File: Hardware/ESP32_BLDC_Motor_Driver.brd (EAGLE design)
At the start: 85.1 x 61 mm, 189 parts, among them J1 USB-C Connector, J2 0532610371, J3 POWER_JACKPOWER_JACK_SLOT, J4 Breadboard Connector, J5 Breadboard Headers, J6 0.1in header, J7 QWIIC_RIGHT_ANGLE, J8 Breakout Header, Q1 20V/4.2A/52mΩ/1.4W, Q2 NPN Transistors, U1 TMC6300, U3 ESP-WROOM-3232D, U4 CH340C, U5 ESD Diode, U6 AP63357, U7 AP2202-ADJ, U8 TMAG5273, U9 LMV324

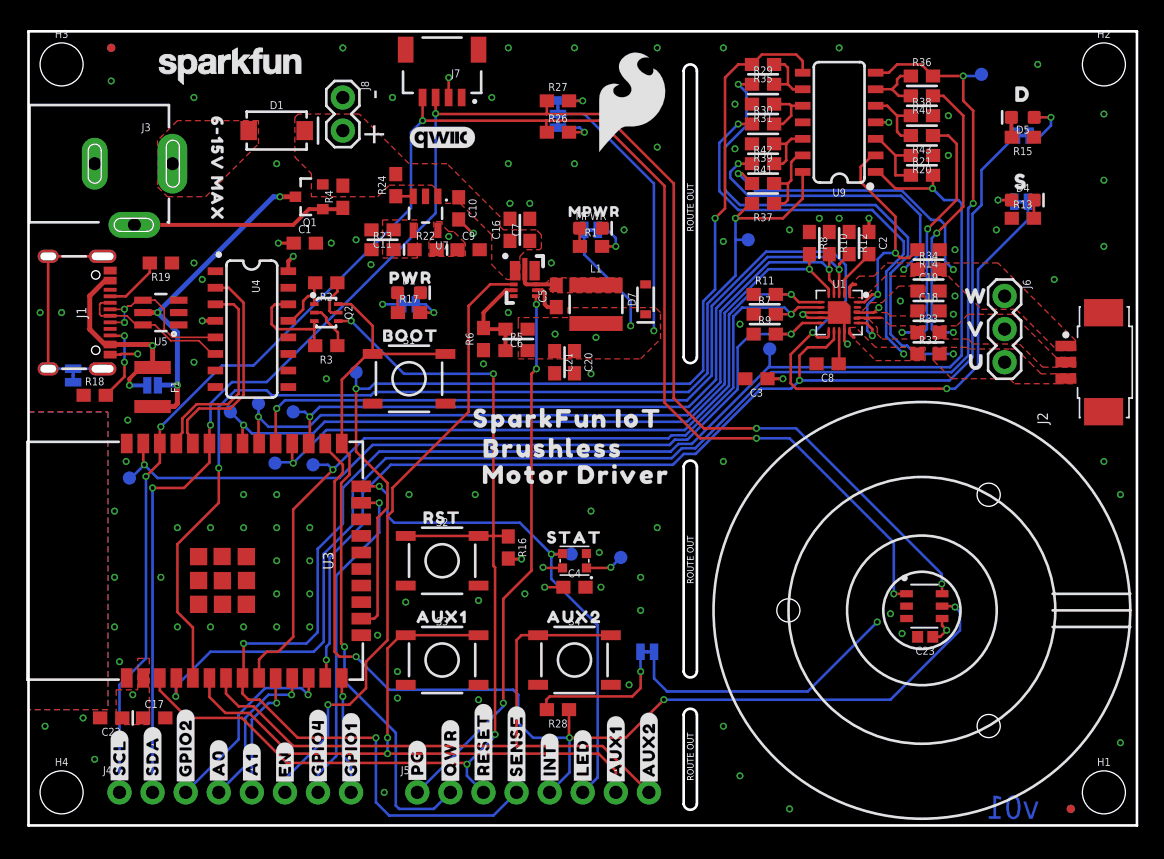
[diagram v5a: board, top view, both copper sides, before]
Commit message: Design review changes
Updated datasheets with correct parts in it now; removed power jack; changed direction of motor and output connector to the motor; swapped resistances of op amp for inline current sensing; updated sizes of some resistances; fixed power scheme of the board; added perfect diode circuit; for more information, see protos review doc
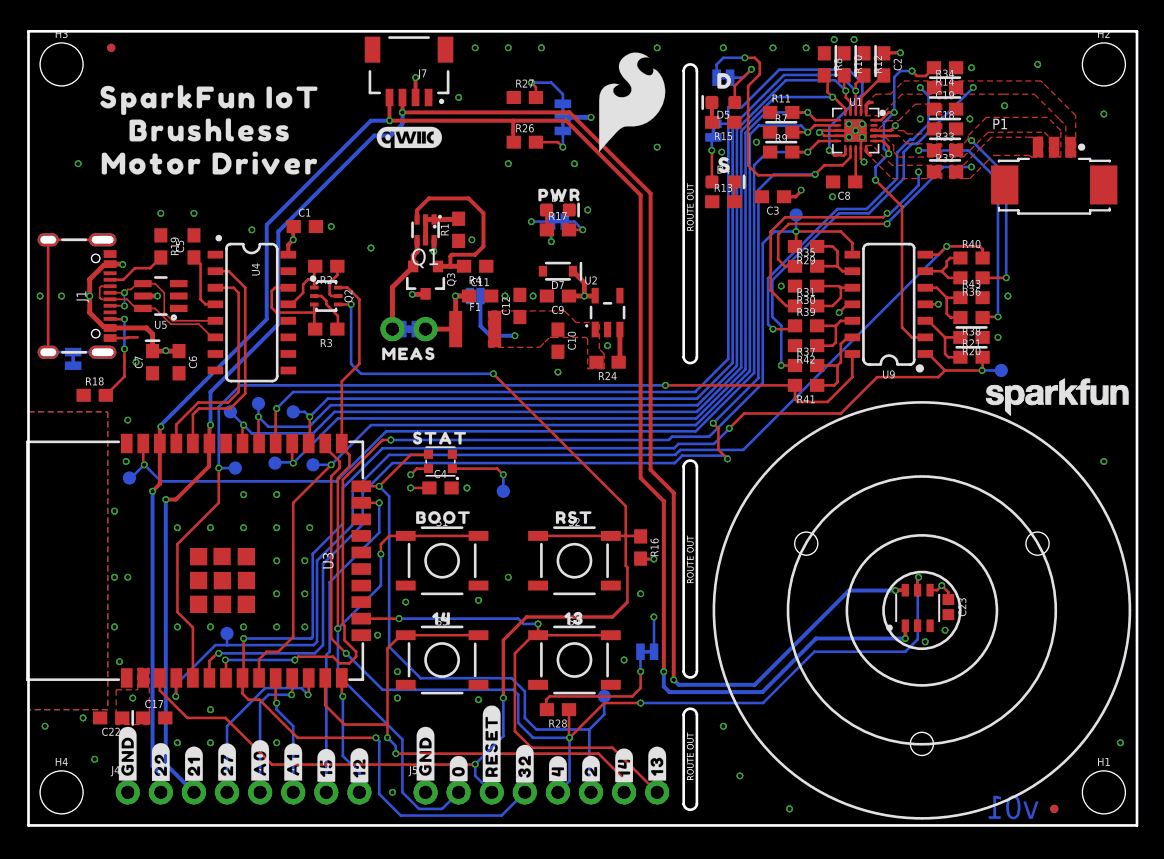
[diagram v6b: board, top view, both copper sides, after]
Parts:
- removed C16: 10uF, SparkFun-Capacitors:0603
- removed C20, C21: 22uF, SparkFun-Capacitors:0603
- removed D1: 1A/40V/500mV, SparkFun-DiscreteSemi:SMA-DIODE
- removed J2: 0532610371, 0532610371:MOLEX_0532610371
- removed J3: POWER_JACKPOWER_JACK_SLOT, SparkFun-Connectors:POWER_JACK_PTH_SLOT
- removed J6: 0.1in header, SparkFun-Connectors:1X03
- removed J8: Breakout Header, SparkFun-Connectors:1X02
- removed L1: 4.7μH, SparkFun-Coils:INDUCTOR_4X4MM
- removed MOTOR: JUMPER-SMT_2_NC_TRACE_SILK, SparkFun-Jumpers:SMT-JUMPER_2_NC_TRACE_SILK
- removed MPWR: RED, SparkFun-LED:LED-0603
- removed R22: 16.2k, SparkFun-Resistors:0603
- removed R23: 26.7k, SparkFun-Resistors:0603
- removed R5: 93.1k, SparkFun-Resistors:0603
- removed R6: 30.1k, SparkFun-Resistors:0603
- removed U$49, U$57: (no value), output:U630063003494
- removed U$50, U$60: (no value), output:V630063003496
- removed U$51, U$61: (no value), output:W630063003497
- removed U$55: (no value), output:#SDA#28
- removed U$58: (no value), output:#SCL#29
- removed U6: AP63357, SparkFun-IC-Power:V-DFN3020-13
- removed U7: AP2202-ADJ, SparkFun-IC-Power:SOT23-5
- added C12: 0.1uF, SparkFun-Capacitors:0603
- added MEAS: JUMPER-COMBO_2_NC_TRACE, SparkFun-Jumpers:COMBO-JUMPER_2_NC_TRACE
- added P1: 0532610371, 0532610371:MOLEX_0532610371
- added Q3: 20V/4.2A/52mΩ/1.4W, SparkFun-DiscreteSemi:SOT23-3
- added U2: 3.3V, SparkFun-IC-Power:SOT23-5
- C11: value 100pF -> 0.1uF
- C5: value 0.1uF -> 10nF
- C6: value 33pF -> 0.1uF
- C7: device SparkFun-Capacitors:0603 -> SparkFun-Capacitors:0603-POLAR
- Q1: value 20V/4.2A/52mΩ/1.4W -> (none); device SparkFun-DiscreteSemi:SOT23-3 -> SparkFun-DiscreteSemi:SOT363_PHILIPS
- R1: value 4.7k -> 100k
- R4: value 100k -> 1M
- U$10: device output:#34#AUX2#21630063003531 -> output:#13_AUX2#36
- U$13: device output:#LED#630063003460 -> output:#GND#32
- U$14: device output:#AUX1#630063003461 -> output:#GND#32
- U$15: device output:#AUX2#630063003461 -> output:#GND#32
- U$18: device output:#INT#8 -> output:#22#33
- U$19: device output:#BYP#630063003471 -> output:#21#33
- U$21: device output:6#15V_MAX0 -> output:#27#33
- U$22: device output:#SENSE#9 -> output:#15#33
- U$3: device output:AUX1630063003521 -> output:1436
- U$31: device output:#QWR#35 -> output:#0#33
- U$33: device output:#PG#30 -> output:#32#33
- U$34: device output:#GPIO1#4 -> output:#4#33
- U$36: device output:#GPIO4#13 -> output:#2#33
- U$38: device output:#MOTOR_EN#16 -> output:#13#36
- U$39: device output:#EN#17 -> output:131437
- U$43: device output:#3V3_PG#31 -> output:#BYP#131439
- U$44: device output:#GPIO2#27 -> output:SPARKFUN_IOT131442
- U$46: device output:SPARKFUN_IOT630063003504 -> output:BRUSHLESS131445
- U$47: device output:BRUSHLESS630063003505 -> output:MOTOR_DRIVER131446
- U$48: device output:MOTOR_DRIVER630063003506 -> output:MEAS131447
- U$6: device output:AUX21630063003526 -> output:#14#AUX1#36
- U$7: device output:MPWR21630063003528 -> output:#12#31
- U$8: device output:#MPWR#21630063003530 -> output:#GND#32
- U$9: device output:#35#AUX1#21630063003534 -> output:#14#36
- moved TP11 72.1 mm to (15.2, 14.7)
- moved LOGO5 68.4 mm to (79.0, 32.9)
- moved U$44 49.9 mm to (14.0, 55.9), turned to 0 degrees
- moved U$7 46.3 mm to (25.4, 4.45), turned to 90 degrees
- moved U$21 45.7 mm to (15.2, 4.70), turned to 90 degrees
- moved U$8 43.9 mm to (30.5, 5.33), flipped to the top, turned to 90 degrees
- moved TP12 43.1 mm to (15.9, 27.4)
- moved U$15 40.0 mm to (7.62, 5.33), flipped to the bottom
- moved U$14 37.5 mm to (7.62, 5.33)
- moved U$45 36.4 mm to (36.8, 30.5)
- moved TP10 35.9 mm to (58.9, 46.9)
- moved U$43 35.8 mm to (34.3, 42.4), turned to 0 degrees
- moved U$46 35.2 mm to (14.0, 53.3)
- moved U$47 34.2 mm to (14.0, 50.8)
- moved U$19 31.0 mm to (12.7, 4.57), flipped to the top, turned to 90 degrees
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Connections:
- removed net 3.3V_A: C1.1, C17.1, C22.1, C4.1, C9.1, J7.2, PWR.2, R16.2, R22.2, STAT.VCC, U3.2, U4.16, U4.4, U7.5
- removed net 3.3V_PG: J5.1, U6.P$5
- removed net BST: C5.1, U6.P$6
- removed net ESP_13/U_OUT: R35.2, TP10.1, U3.16, U9.8
- removed net ESP_14/DIAG: D.2, U1.12, U3.13
- removed net ESP_34/AUX1: J5.7, S3.1, S3.2, U3.6
- removed net ESP_35/AUX2: J5.8, S4.1, S4.2, U3.7
- removed net FB: C6.2, R5.1, R6.2, U6.P$3
- removed net LDO_EN: R24.1, U7.3
- removed net MOTOR_EN: J4.6, U6.P$2
- removed net N$23: MOTOR.1, R1.2
- removed net N$34: MPWR.A, R1.1
- removed net N$5: J3.GNDBREAK, Q1.1, R4.1
- removed net POWER_IN: D1.A, J3.PWR
- removed net SW: C5.2, L1.P$1, U6.P$7, U6.P$9
- removed net VIN: C10.1, C16.1, C7.1, D1.C, J8.2, Q1.2, R24.2, R4.2, U6.P$1, U7.1
- new net 5V: BYP.2, C10.1, C12.1, F1.2, R24.2, U2.1
- new net 5V_MEAS: MEAS.1, MEAS.3, Q1.4, Q3.2
- new net ESP_13/AUX2: J5.8, S4.1, S4.2, U3.16
- new net ESP_14/AUX1: J5.7, S3.1, S3.2, U3.13
- new net ESP_21/TP_SDA1: R27.1
- new net ESP_34/DIAG: D.2, U1.12, U3.6
- new net ESP_35/U_OUT: R29.2, TP10.1, U3.7, U9.8
- new net N$21: Q1.3, Q3.1, R4.2
- new net N$22: Q1.1, Q1.2, Q1.5, R1.2
- new net N$6: R24.1, U2.3
- net 3.3V: now also C1.1, C17.1, C22.1, C4.1, C9.1, J7.2, PWR.2, R16.2, STAT.VCC, U2.5, U3.2, U4.16; no longer C20.1, C21.1, C6.1, L1.P$2, MOTOR.2, R5.2
- net ESP_21/TP_SDA: now also J4.3; no longer J4.2, R27.1
- net ESP_22/TP_SCL: now also J4.2; no longer J4.1
- net ESP_25/TP_A1: now also J4.6; no longer J4.5
- net ESP_26/TP_A0: now also J4.5; no longer J4.4
- net ESP_27/GPIO2: now also J4.4; no longer J4.3
- net ESP_36/V_OUT: now also R40.2; no longer R36.2
- net ESP_39/W_OUT: now also R41.2; no longer R37.2
- net GND: now also C12.2, C5.2, C6.2, C7.-, J4.1, J5.1, R1.1, R30.2, R4.1, R42.2, R43.2, U2.2; no longer C16.2, C20.2, C21.2, C7.2, J3.GND, J8.1, MPWR.C, R23.1, R31.2, R38.2, R39.2, R6.1, U6.P$4, U6.P$8, U7.2
- net N$16: now also R29.1, R35.2; no longer R29.2, R35.1
- net N$17: now also C11.1, MEAS.2, MEAS.4; no longer J1.VBUS1, J1.VBUS2
- net N$18: now also R30.1, R31.2; no longer R30.2, R31.1
- net N$19: now also R36.2, R40.1; no longer R36.1, R40.2
- net N$2: now also C5.1, U4.4; no longer C11.1, R22.1, R23.2, U7.4
- net N$20: now also R38.2, R43.1; no longer R38.1, R43.2
- net N$24: now also R37.2, R41.1; no longer R37.1, R41.2
- net N$25: now also R39.2, R42.1; no longer R39.1, R42.2
- net SENSE_U: now also R31.1; no longer R30.1
- net SENSE_V: now also R38.1; no longer R43.1
- net SENSE_W: now also R39.1; no longer R42.1
- net U: now also P1.3, R35.1; no longer J2.3, J6.3, R29.1
- net V: now also P1.2, R36.1; no longer J2.2, J6.2, R40.1
- net V_USB: now also C6.1, C7.+, J1.VBUS1, J1.VBUS2, Q1.6, Q3.3; no longer BYP.2, F1.2, Q1.3
- net W: now also P1.1, R37.1; no longer J2.1, J6.1, R41.1
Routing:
- net ESP_34/DIAG: track 0.00 -> 102.5 mm, vias 0 -> 5
- net ESP_14/DIAG: track 90.7 -> 0.00 mm, vias 2 -> 0
- net ESP_35/U_OUT: track 0.00 -> 83.0 mm, vias 0 -> 4
- net ESP_13/U_OUT: track 79.5 -> 0.00 mm, vias 2 -> 0
- net ESP_35/AUX2: track 52.3 -> 0.00 mm
- net ESP_34/AUX1: track 52.1 -> 0.00 mm, vias 2 -> 0
- net MOTOR_EN: track 48.3 -> 0.00 mm, vias 1 -> 0
- net ESP_14/AUX1: track 0.00 -> 42.6 mm, vias 0 -> 2
- net 3.3V_PG: track 41.9 -> 0.00 mm, vias 3 -> 0
- net ESP_13/AUX2: track 0.00 -> 41.4 mm, vias 0 -> 2
- net 3.3V: track 58.9 -> 28.1 mm, vias 11 -> 18
- net ESP_36/V_OUT: track 109.8 -> 86.9 mm, vias 3 -> 2
- net U: track 39.1 -> 20.4 mm
- net ESP_5/!STDBY: track 97.3 -> 79.4 mm, vias 3 -> 2
- net N$5: track 16.5 -> 0.00 mm
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- added copper zone on layer 1, net 5V
- added copper zone on layer 15, net V_USB
- removed copper zone on layer 1, net 3.3V_A
- removed copper zone on layer 15, net 3.3V_A
- removed copper zone on layer 1, net N$2
- removed copper zone on layer 1, net POWER_IN
- removed copper zone on layer 1, net SW
- removed copper zone on layer 1, net VIN
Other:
- board text removed: "+"
- board text removed: "-"

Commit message: Design Review Changes
Added back in AP63557 circuit for more power to motor; Adjusted trace size for better differential pairs and power usage; created standoff board for the motor to sit on while moving; see design notes for more information.
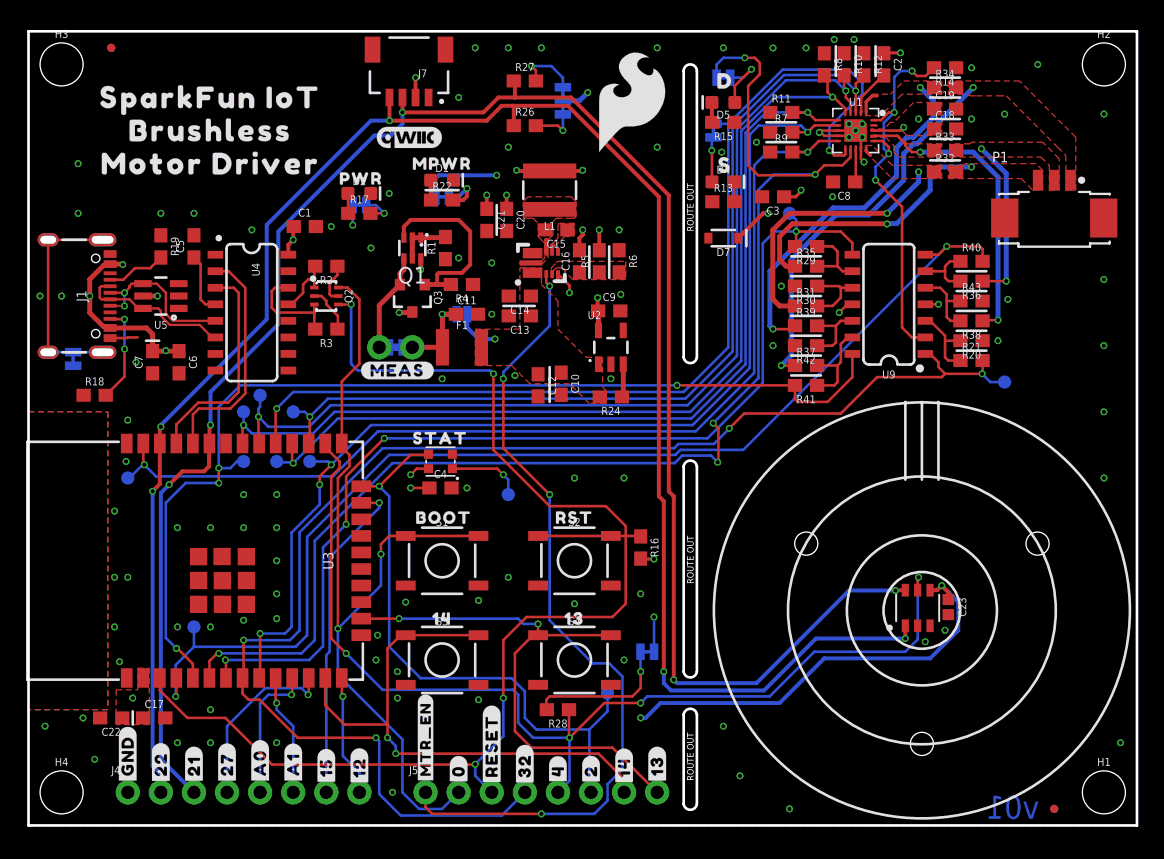
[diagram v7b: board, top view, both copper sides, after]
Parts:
- removed LOGO5: SFE_LOGO_NAME.1_INCH, SparkFun-Aesthetics:SFE_LOGO_NAME_.1
- removed U$59: (no value), output:SPARKFUN_IOT_BRUSHLESS630063003514
- added C13, C14: 10uF, SparkFun-Capacitors:0603
- added C15: 0.1uF, SparkFun-Capacitors:0603
- added C16: 33pF, SparkFun-Capacitors:0603
- added C20, C21: 22uF, SparkFun-Capacitors:0603
- added D1: RED, SparkFun-LED:LED-0603
- added L1: 4.7μH, SparkFun-Coils:INDUCTOR_4X4MM
- added MPWR: JUMPER-SMT_2_NC_TRACE_SILK, SparkFun-Jumpers:SMT-JUMPER_2_NC_TRACE_SILK
- added R22: 4.7k, SparkFun-Resistors:0603
- added R5: 93.1k, SparkFun-Resistors:0603
- added R6: 30.1k, SparkFun-Resistors:0603
- added U$49: (no value), output:MPWR131449
- added U$50: (no value), output:#MEAS#131453
- added U$51: (no value), output:#MTR_EN#131460
- added U$55: (no value), output:IOT_BRUSHLESS131454
- added U6: AP63357, SparkFun-IC-Power:V-DFN3020-13
- U$13: device output:#GND#32 -> output:#MTR_EN#131458
- U$20: device output:#D#630063003474 -> output:#MPWR#131468
- U$28: device output:#S#630063003475 -> output:##STBY##131466
- U$48: device output:MEAS131447 -> output:#MEAS#131453
- U$8: device output:#GND#32 -> output:#DIAG#131461
- moved U$8 58.5 mm to (53.3, 59.2), flipped to the bottom, turned to 0 degrees
- moved U$20 23.3 mm to (31.9, 50.0)
- moved D2 15.3 mm to (25.4, 48.5)
- moved PWR 15.3 mm to (25.4, 47.6)
- moved R17 15.3 mm to (25.4, 47.0)
- moved U$12 15.3 mm to (25.5, 49.7)
- moved U$27 15.3 mm to (25.4, 49.4)
- moved D7 13.0 mm to (53.3, 45.1)
- moved C12 6.25 mm to (39.1, 33.8), turned to 270 degrees
- moved C9 4.10 mm to (44.6, 39.5), turned to 0 degrees
- moved C10 3.31 mm to (40.9, 33.9)
- moved R24 2.68 mm to (44.7, 32.9)
- moved U2 2.68 mm to (44.7, 36.7)
- moved TP11 2.59 mm to (12.7, 15.2)
- moved P1 2.54 mm to (78.7, 49.5)
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- renumbered D to DIAG, S to !STBY
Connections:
- removed net ESP_21/TP_SDA1: R27.1
- new net 3.3V_A: C16.2, C18.1, C19.1, C2.1, C20.1, C21.1, C3.1, D7.C, L1.P$2, MPWR.2, R5.2, U1.18, U9.4
- new net 3.3V_PG: U6.P$5
- new net BST: C15.1, U6.P$6
- new net FB: C16.1, R5.1, R6.2, U6.P$3
- new net MOTOR_EN: J5.1, U6.P$2
- new net N$26: D1.A, R22.1
- new net N$27: MPWR.1, R22.2
- new net SW: C15.2, L1.P$1, U6.P$7, U6.P$9
- net 3.3V: no longer C18.1, C19.1, C2.1, C3.1, D7.C, U1.18, U9.4
- net 5V: now also C13.1, C14.1, U6.P$1
- net ESP_21/TP_SDA: now also R27.1
- net GND: now also C13.2, C14.2, C20.2, C21.2, D1.C, R6.1, U6.P$4, U6.P$8; no longer J5.1
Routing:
- net MOTOR_EN: track 0.00 -> 62.8 mm, vias 0 -> 4
- net 3.3V_A: track 0.00 -> 26.0 mm, vias 0 -> 13
- net 3.3V: track 28.1 -> 50.3 mm, vias 18 -> 13
- net ESP_21/TP_SDA: track 143.6 -> 147.3 mm
- net N$27: track 0.00 -> 3.42 mm, vias 0 -> 1
- net ESP_39/W_OUT: track 76.9 -> 80.0 mm, vias 2 -> 4
- net ESP_35/U_OUT: track 83.0 -> 80.1 mm
- net SENSE_V: track 20.5 -> 23.1 mm
- net !RESET: track 97.8 -> 100.3 mm
- net GND: track 11.9 -> 14.2 mm, vias 94 -> 102
- net 5V: track 5.26 -> 3.53 mm
- net N$26: track 0.00 -> 1.54 mm
- net ESP_22/TP_SCL: track 145.1 -> 146.5 mm
- net ESP_34/DIAG: track 102.5 -> 101.2 mm
- net ESP_5/!STDBY: track 79.4 -> 78.1 mm
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- added copper zone on layer 1, net 3.3V_A
- added copper zone on layer 15, net 3.3V_A
- added copper zone on layer 1, net BST
- added copper zone on layer 1, net FB
- added copper zone on layer 1, net SW

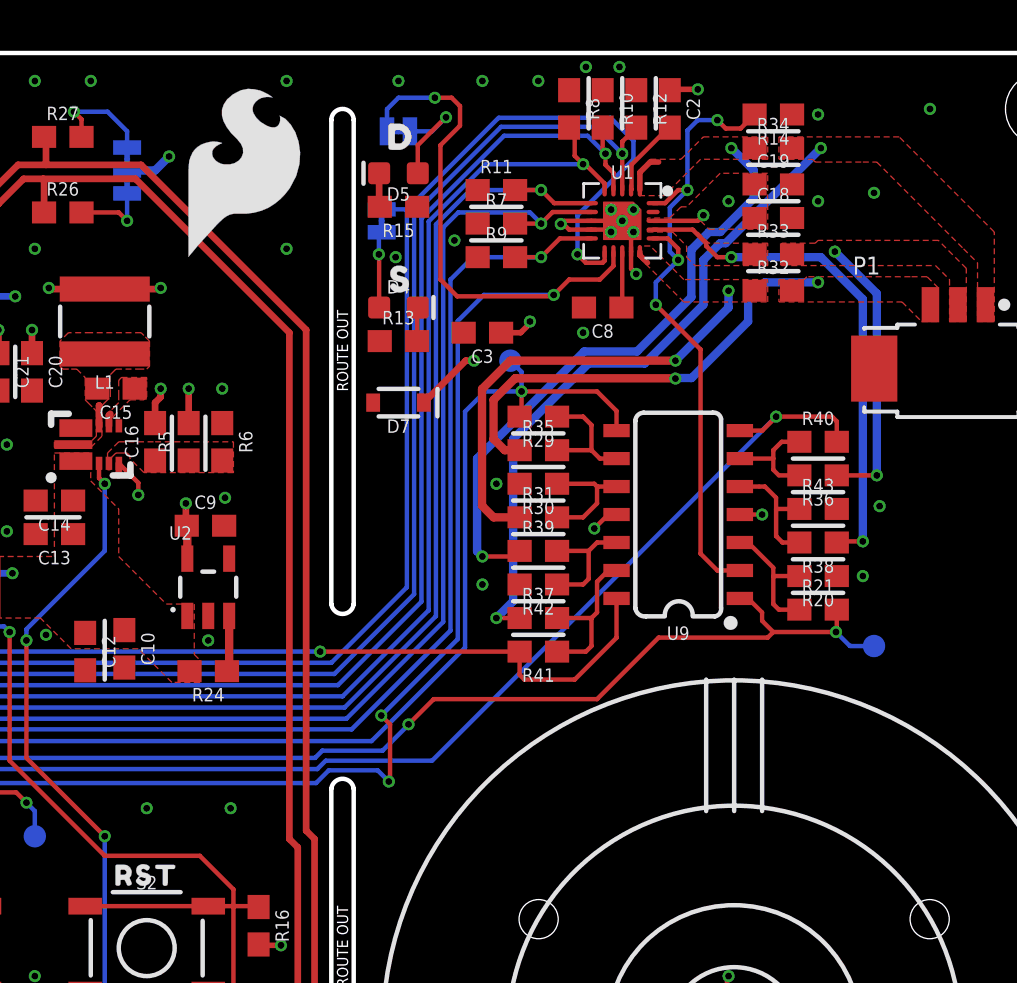
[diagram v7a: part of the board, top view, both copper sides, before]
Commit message: Final design changes made; files for ordering added
Made final adjustments with Alex - check document for more information on small adjustments; ran CAM script for output files for board; also made output CAM files for standoff to be ordered as well.
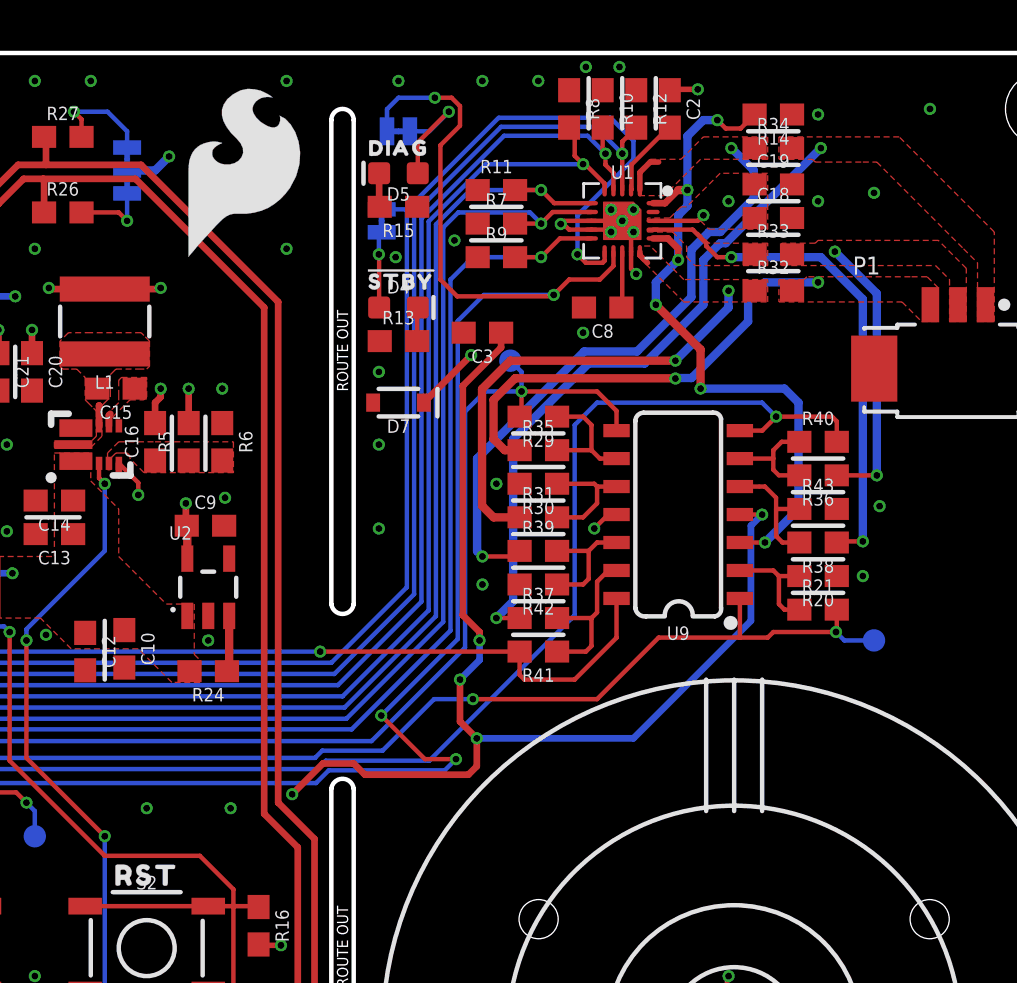
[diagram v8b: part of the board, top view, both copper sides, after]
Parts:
- removed U$28: (no value), output:##STBY##131466
- added U$57: (no value), output:DIAG131469
- R20: value 1.5k -> 1k
- U$10: device output:#13_AUX2#36 -> output:##STBY##16
- U$52: device output:S630063003507 -> output:#13#AUX2#14
- U$53: device output:D630063003508 -> output:#STBY#131470
- U$8: device output:#DIAG#131461 -> output:#DIAG#15
- moved U$10 46.9 mm to (56.0, 53.5), turned to 0 degrees
- moved U$52 43.9 mm to (48.3, 7.11), flipped to the bottom, turned to 90 degrees
- moved U$53 6.48 mm to (53.5, 50.7)
- moved U$8 3.86 mm to (56.8, 57.4)
- moved TP9 0.25 mm to (74.9, 34.3)
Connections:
- net 3.3V: now also C3.1, U9.4
- net 3.3V_A: no longer C3.1, U9.4
- net N$14: now also U9.2; no longer U9.3
- net SENSE: now also U9.3; no longer U9.2
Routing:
- net 3.3V: track 50.3 -> 101.7 mm, vias 13 -> 18
- net ESP_36/V_OUT: track 88.0 -> 93.6 mm
- net ESP_34/DIAG: track 101.2 -> 105.3 mm
- net SENSE: track 30.4 -> 33.1 mm, vias 4 -> 6
- net 3.3V_A: track 26.0 -> 23.4 mm, vias 13 -> 11
- net N$14: track 6.11 -> 5.11 mm
- net ESP_32/CURR_SENSE: track 107.8 -> 107.1 mm
- net D: track 4.98 -> 5.52 mm
- net GND: vias 102 -> 105
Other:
- board text added: "Units in inches"
